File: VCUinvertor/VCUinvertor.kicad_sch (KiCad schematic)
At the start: 101 parts, among them J1 NXP1, J2 Conn_02x10_Odd_Even, J3 NXP2, J4 Conn_02x10_Odd_Even, J5 Conn_02x10_Odd_Even, J6 Conn_02x10_Odd_Even, J7 PowerSupply, J8 CAN_NXP, J9 BACKLIGHT, Q1 BSS138, Q10 BSS138, Q2 BSS138, Q3 BSS138, Q4 BSS138, Q5 BSS138, Q6 BSS138, Q7 BSS138, Q8 BSS138, Q9 BSS138, U1 TJA1448ATK, U2 REF3433T, U3 TLV76150DCY

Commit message: Layout_Invertor2
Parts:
- removed R37: 10k, symbol Device:R_Small
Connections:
- net BACKLIGHT_ON: now also J4.20 (Pin_20)
- net NXP_ACC01: now also J4.10 (Pin_10)
- net NXP_ACC02: now also J6.2 (Pin_2)
- net NXP_BRK01: now also J4.14 (Pin_14)
- net NXP_BRK02: now also J6.6 (Pin_6)
- net NXP_ECO01: now also J4.12 (Pin_12)
- net NXP_ECO02: now also J6.4 (Pin_4)
- net NXP_FWD01: now also J4.16 (Pin_16)
- net NXP_FWD02: now also J6.8 (Pin_8)
- net NXP_REV01: now also J4.18 (Pin_18)
- net NXP_REV02: now also J6.10 (Pin_10)
- net NXP_TPSOUT01: now also J3.18 (Pin_18)
- net NXP_TPSOUT02: now also J3.20 (Pin_20)
- net PWM_NXP1: now also J4.8 (Pin_8)
- net PWM_NXP2: now also J4.6 (Pin_6)
- net PWM_NXP3: now also J4.4 (Pin_4)
- net PWM_NXP4: now also J4.2 (Pin_2)
- net Pxx: now also J3.2 (Pin_2)
- net Pyy: now also J3.4 (Pin_4)
- net RX0: now also J3.8 (Pin_8)
- net RX1: now also J3.12 (Pin_12)
- net TX0: now also J3.6 (Pin_6)
- net TX1: now also J3.10 (Pin_10)
- net H_Brk2: now reaches Q8.3 (D), R20.1
- net H_Brk2: no longer JO25.1 (Pin_1)
- net FWD2: now reaches Q9.3 (D), R22.1
- net FWD2: no longer JO23.1 (Pin_1)
- net ACC2: now reaches Q6.3 (D), R15.1
- net ACC2: no longer JO31.1 (Pin_1)
- net REV2: now reaches Q10.3 (D), R24.1
- net REV2: no longer JO22.1 (Pin_1)
- net ECO2: now reaches Q7.3 (D), R17.1
- net ECO2: no longer JO29.1 (Pin_1)
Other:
- note added: "To be simulated"
- moved on the sheet: JO21, JO22, JO23, JO24, JO25, JO26, JO27, JO28, JO29, JO31, JO33, JO34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

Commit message: NMOS_Simulation_Selection
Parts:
- removed R29, R30, R31, R32, R33, R34, R35, R36, R38: 10k, symbol Device:R_Small
- added R10, R11, R12, R13, R14: 5k, symbol Device:R_Small
- R16, R18, R20, R22, R24: value 10k -> 5k
- R5, R6, R7, R8, R9: value 5k -> 10k
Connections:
- net ACC2: now also R16.2; no longer R15.1
- net ECO2: now also R18.2; no longer R17.1
- net FWD2: now also R22.2; no longer R22.1
- net GND: now also R5.2, R6.2, R7.2, R8.2, R9.2; no longer R16.2, R18.2, R20.2, R22.2, R24.2
- net H_Brk2: now also R20.2; no longer R20.1
- net NXP_ACC01: now also R14.1
- net NXP_ACC02: now also R15.1
- net NXP_BRK01: now also R11.1
- net NXP_BRK02: now also R20.1
- net NXP_ECO01: now also R10.1
- net NXP_ECO02: now also R17.1
- net NXP_FWD01: now also R12.1
- net NXP_FWD02: now also R22.1
- net NXP_REV01: now also R13.1
- net NXP_REV02: now also R24.1
- net REV2: now also R24.2; no longer R24.1
- net at JO19.1 (Pin_1), Q1.3 (D): now also R14.2; no longer R5.2
- net at JO3.1 (Pin_1), Q5.3 (D): now also R13.2; no longer R9.2
- net at JO11.1 (Pin_1), Q2.3 (D): now also R10.2; no longer R6.2
- net at JO5.1 (Pin_1), Q4.3 (D): now also R12.2; no longer R8.2
- net at JO9.1 (Pin_1), Q3.3 (D): now also R11.2; no longer R7.2
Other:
- note removed: "To be simulated"

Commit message: Footprint assignment
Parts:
- C1, C10, C11, C2, C3, C4, C5, C6, C7, C8, C9: footprint (none) -> Capacitor_SMD:C_0805_2012Metric_Pad1.18x1.45mm_HandSolder
- DAC1: footprint LTC2645HMS-L12_PBF:MSOP-16_MS -> Package_SO:MSOP-16-1EP_3x4.039mm_P0.5mm_EP1.651x2.845mm
- J1: value NXP1 -> NXP12
- J2: value Conn_02x10_Odd_Even -> NXP11
- J3: value NXP2 -> NXP15
- J4: value Conn_02x10_Odd_Even -> NXP14
- J5: value Conn_02x10_Odd_Even -> NXP10
- J6: value Conn_02x10_Odd_Even -> NXP13
- R1, R10, R11, R12, R13, R14, R15, R16, R17, R18, R19, R2, R20, R21, R22, R23, R24, R25, R26, R27, R28, R3, R4, R5, R6, R7, R8, R9: footprint (none) -> Resistor_SMD:R_0805_2012Metric
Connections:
- net +12V: now also J6.15 (Pin_15)
- net ACC2: now also JO31.1 (Pin_1)
- net ECO2: now also JO29.1 (Pin_1)
- net FWD2: now also JO23.1 (Pin_1)
- net GND: now also J6.13 (Pin_13)
- net H_Brk2: now also JO25.1 (Pin_1)
- net REV2: now also JO22.1 (Pin_1)
- net ACC1: now reaches JO19.1 (Pin_1), Q1.3 (D), R14.2
- net FWD1: now reaches JO5.1 (Pin_1), Q4.3 (D), R12.2
- net ECO1: now reaches JO11.1 (Pin_1), Q2.3 (D), R10.2
- net H_Brk1: now reaches JO9.1 (Pin_1), Q3.3 (D), R11.2
- net REV1: now reaches JO3.1 (Pin_1), Q5.3 (D), R13.2
- no-connect marks 9 -> 103
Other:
- note added: "J13 - 1 & 15 (12V) J13 - 13 (GND)"
- moved on the sheet: CA1, JO1, JO11, JO13, JO14, JO15, JO19, JO21, JO22, JO23, JO24, JO25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

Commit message: Layout_Global arrangement
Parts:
- J8: footprint (none) -> Connector_PinHeader_2.54mm:PinHeader_1x04_P2.54mm_Vertical
- J9: footprint (none) -> Connector_JST:JST_PH_B3B-PH-K_1x03_P2.00mm_Vertical
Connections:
- net GND: no longer JO26.1 (Pin_1), JO6.1 (Pin_1)
- net Brk_AN2: now reaches DAC1.14 (VOUTC), JO30.1 (Pin_1)
- net Brk_AN1: now reaches DAC1.2 (VOUTA), JO10.1 (Pin_1)
- no-connect marks 103 -> 105
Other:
- moved on the sheet: JO1, JO10, JO11, JO12, JO13, JO15, JO19, JO21, JO22, JO23, JO24, JO25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

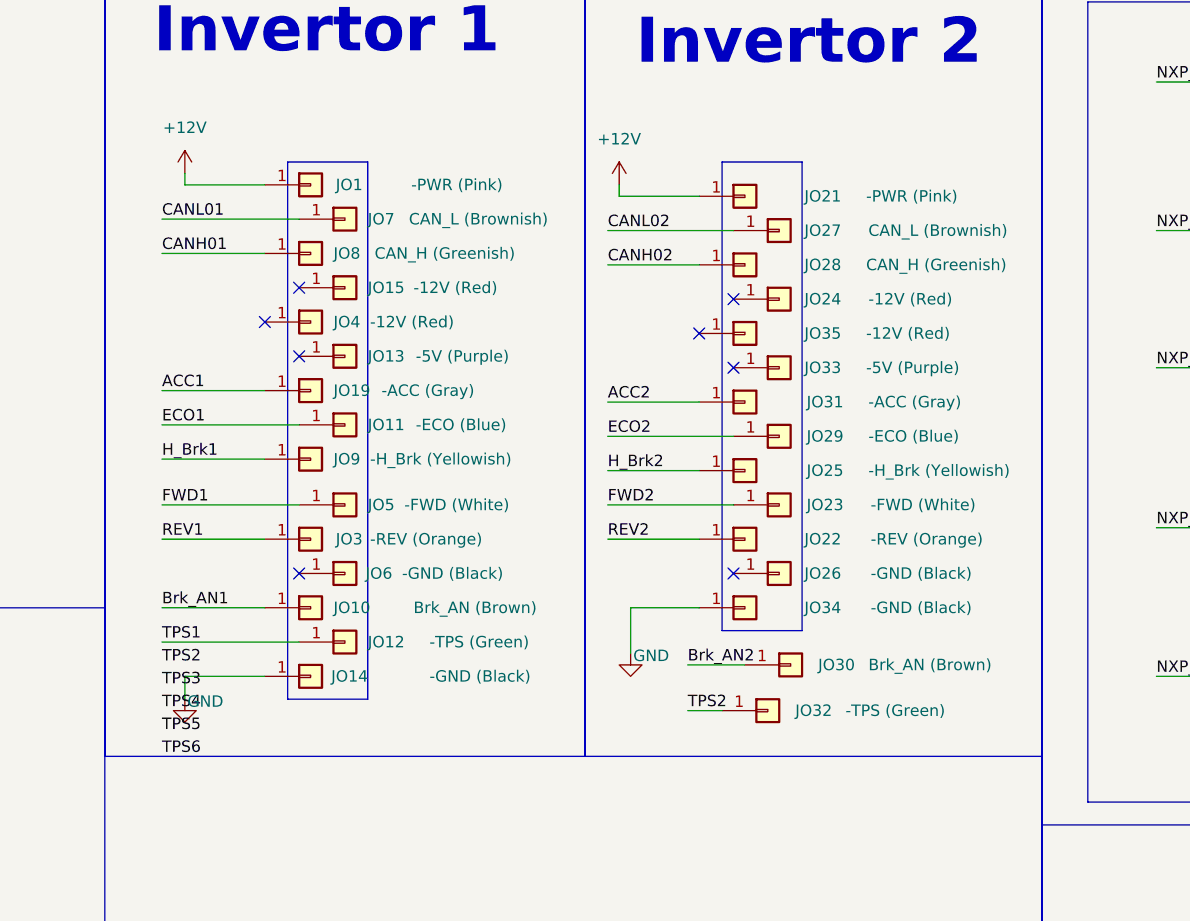
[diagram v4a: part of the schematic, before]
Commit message: DAQ footprint correction
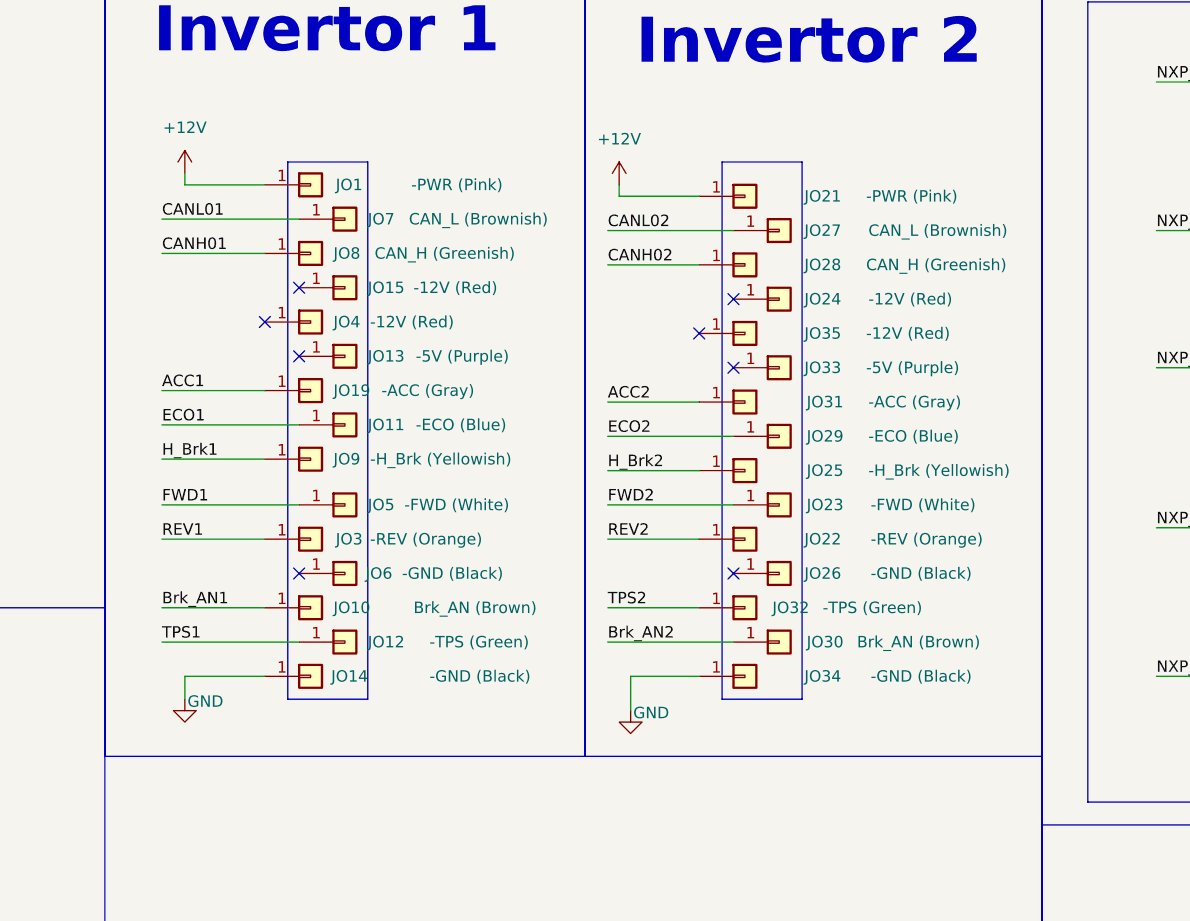
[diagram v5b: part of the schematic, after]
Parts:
- DAC1: footprint Package_SO:MSOP-16-1EP_3x4.039mm_P0.5mm_EP1.651x2.845mm -> LTC2645HMS-L12_PBF:MSOP-16_MS
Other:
- moved on the sheet: JO30, JO32, JO34
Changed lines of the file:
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@@
 	(rectangle
 		(start 236.22 142.24)
-		(end 245.11 194.31)
+		(end 245.11 201.93)
 		(stroke
 			(width 0)
@@
 	(wire
 		(pts
-			(xy 232.41 198.12) (xy 238.76 198.12)
-		)
-		(stroke
-			(width 0)
-			(type default)
-		)
-	)
-	(wire
-		(pts
 			(xy 312.42 133.35) (xy 314.96 133.35)
 		)
@@
 	(wire
 		(pts
-			(xy 226.06 191.77) (xy 226.06 196.85)
+			(xy 226.06 199.39) (xy 226.06 203.2)
 		)
 		(stroke
@@
 	(wire
 		(pts
+			(xy 223.52 195.58) (xy 237.49 195.58)
+		)
+		(stroke
+			(width 0)
+			(type default)
+		)
+	)
+	(wire
+		(pts
 			(xy 203.2 83.82) (xy 203.2 85.09)
 		)
@@
 	(wire
 		(pts
-			(xy 232.41 203.2) (xy 236.22 203.2)
+			(xy 223.52 191.77) (xy 233.68 191.77)
 		)
 		(stroke
@@
 	(wire
 		(pts
-			(xy 226.06 191.77) (xy 233.68 191.77)
+			(xy 226.06 199.39) (xy 233.68 199.39)
 		)
 		(stroke
@@
 		)
 	)
-	(label "TPS4"
-		(at 173.99 203.2 0)
-		(effects
-			(font
-				(size 1.27 1.27)
-			)
-			(justify left bottom)
-		)
-	)
 	(label "H_Brk2"
 		(at 223.52 176.53 0)
@@
 		)
 	)
-	(label "TPS2"
-		(at 173.99 198.12 0)
-		(effects
-			(font
-				(size 1.27 1.27)
-			)
-			(justify left bottom)
-		)
-	)
 	(label "REV1"
 		(at 173.99 184.15 0)
@@
 		)
 	)
-	(label "TPS3"
-		(at 173.99 200.66 0)
-		(effects
-			(font
-				(size 1.27 1.27)
-			)
-			(justify left bottom)
-		)
-	)
 	(label "NXP_ECO01"
 		(at 121.92 119.38 0)
@@
 	)
 	(label "TPS2"
-		(at 232.41 203.2 0)
+		(at 223.52 191.77 0)
 		(effects
 			(font
@@
 		)
 	)
-	(label "TPS5"
-		(at 173.99 205.74 0)
-		(effects
-			(font
-				(size 1.27 1.27)
-			)
-			(justify left bottom)
-		)
-	)
 	(label "NXP_ACC01"
 		(at 284.48 133.35 0)
@@
 	)
 	(label "Brk_AN2"
-		(at 232.41 198.12 0)
+		(at 223.52 195.58 0)
 		(effects
 			(font
@@
 		)
 	)
-	(label "TPS6"
-		(at 173.99 208.28 0)
-		(effects
-			(font
-				(size 1.27 1.27)
-			)
-			(justify left bottom)
-		)
-	)
 	(label "V+"
 		(at 48.26 224.79 0)
@@
 	(symbol
 		(lib_id "Connector_Generic:Conn_01x01")
-		(at 238.76 191.77 0)
+		(at 238.76 199.39 0)
 		(unit 1)
 		(exclude_from_sim no)
@@
 		(dnp no)
 		(property "Reference" "JO34"
-			(at 245.364 191.77 0)
+			(at 245.364 199.39 0)
 			(effects
 				(font
@@
 		)
 		(property "Value" "-GND (Black)"
-			(at 252.73 191.77 0)
+			(at 252.73 199.39 0)
 			(effects
 				(font
@@
 		)
 		(property "Footprint" "Connector_Wire:SolderWire-0.75sqmm_1x01_D1.25mm_OD2.3mm"
-			(at 238.76 191.77 0)
+			(at 238.76 199.39 0)
 			(effects
 				(font
@@
 		)
 		(property "Datasheet" "~"
-			(at 238.76 191.77 0)
+			(at 238.76 199.39 0)
 			(effects
 				(font
@@
 		)
 		(property "Description" "Generic connector, single row, 01x01, script generated (kicad-library-utils/schlib/autogen/connector/)"
-			(at 238.76 191.77 0)
+			(at 238.76 199.39 0)
 			(effects
 				(font
@@
 			)
 		)
-		(property "Footprint" "Package_SO:MSOP-16-1EP_3x4.039mm_P0.5mm_EP1.651x2.845mm"
+		(property "Footprint" "LTC2645HMS-L12_PBF:MSOP-16_MS"
 			(at 325.12 31.496 0)
 			(effects
@@
 		)
 		(instances
-			(project ""
+			(project "VCUinvertor"
 				(path "/2b4b6758-f217-4dbc-8f9c-9ada5d4e488c"
 					(reference "DAC1")
@@
 	(symbol
 		(lib_id "power:GND")
-		(at 226.06 196.85 0)
+		(at 226.06 203.2 0)
 		(unit 1)
 		(exclude_from_sim no)
@@
 		(dnp no)
 		(property "Reference" "#PWR015"
-			(at 226.06 203.2 0)
+			(at 226.06 209.55 0)
 			(effects
 				(font
@@
 		)
 		(property "Value" "GND"
-			(at 228.346 197.104 0)
+			(at 228.346 203.454 0)
 			(effects
 				(font
@@
 		)
 		(property "Footprint" ""
-			(at 226.06 196.85 0)
+			(at 226.06 203.2 0)
 			(effects
 				(font
@@
 		)
 		(property "Datasheet" ""
-			(at 226.06 196.85 0)
+			(at 226.06 203.2 0)
 			(effects
 				(font
@@
 		)
 		(property "Description" "Power symbol creates a global label with name \"GND\" , ground"
-			(at 226.06 196.85 0)
+			(at 226.06 203.2 0)
 			(effects
 				(font
@@
 	(symbol
 		(lib_id "Connector_Generic:Conn_01x01")
-		(at 243.84 198.12 0)
+		(at 242.57 195.58 0)
 		(unit 1)
 		(exclude_from_sim no)
@@
 		(dnp no)
 		(property "Reference" "JO30"
-			(at 246.888 198.12 0)
+			(at 245.618 195.58 0)
 			(effects
 				(font
@@
 		)
 		(property "Value" "Brk_AN (Brown)"
-			(at 252.476 198.12 0)
+			(at 251.206 195.58 0)
 			(effects
 				(font
@@
 		)
 		(property "Footprint" "Connector_Wire:SolderWire-0.75sqmm_1x01_D1.25mm_OD2.3mm"
-			(at 243.84 198.12 0)
+			(at 242.57 195.58 0)
 			(effects
 				(font
@@
 		)
 		(property "Datasheet" "~"
-			(at 243.84 198.12 0)
+			(at 242.57 195.58 0)
 			(effects
 				(font
@@
 		)
 		(property "Description" "Generic connector, single row, 01x01, script generated (kicad-library-utils/schlib/autogen/connector/)"
-			(at 243.84 198.12 0)
+			(at 242.57 195.58 0)
 			(effects
 				(font
@@
 				(font
 					(size 1.27 1.27)
+					(color 40 205 44 1)
 				)
 				(justify left)
@@
 	(symbol
 		(lib_id "Connector_Generic:Conn_01x01")
-		(at 241.3 203.2 0)
+		(at 238.76 191.77 0)
 		(unit 1)
 		(exclude_from_sim no)
@@
 		(dnp no)
 		(property "Reference" "JO32"
-			(at 244.348 203.2 0)
+			(at 241.808 191.77 0)
 			(effects
 				(font
@@
 		)
 		(property "Value" "-TPS (Green)"
-			(at 249.936 203.2 0)
+			(at 247.396 191.77 0)
 			(effects
 				(font
 					(size 1.27 1.27)
+					(color 40 205 44 1)
 				)
 				(justify left)
@@
 		)
 		(property "Footprint" "Connector_Wire:SolderWire-0.75sqmm_1x01_D1.25mm_OD2.3mm"
-			(at 241.3 203.2 0)
+			(at 238.76 191.77 0)
 			(effects
 				(font
@@
 		)
 		(property "Datasheet" "~"
-			(at 241.3 203.2 0)
+			(at 238.76 191.77 0)
 			(effects
 				(font
@@
 		)
 		(property "Description" "Generic connector, single row, 01x01, script generated (kicad-library-utils/schlib/autogen/connector/)"
-			(at 241.3 203.2 0)
+			(at 238.76 191.77 0)
 			(effects
 				(font
